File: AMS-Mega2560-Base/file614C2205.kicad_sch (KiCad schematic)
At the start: 3 parts, among them IC1 CD74HC4050ME4, IC2 CD74HC4050ME4, J8 Conn_01x03

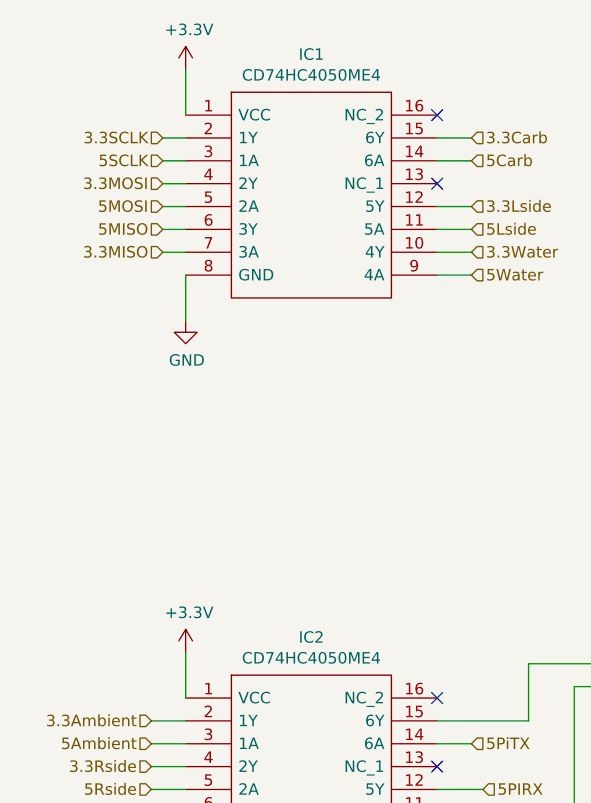
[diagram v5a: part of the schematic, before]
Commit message: WIP for power on input and RTC battery switch over.
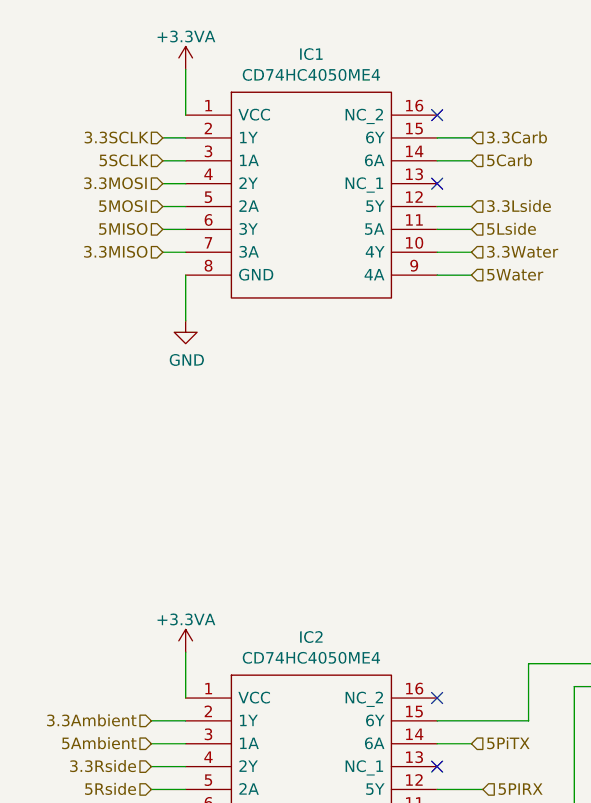
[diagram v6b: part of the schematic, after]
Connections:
- net +3V3 renamed +3.3VA
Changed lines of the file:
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@@
     (pin "9")
-  )
-  (symbol (lib_id "power:+3.3V") (at 53.34 33.02 0) (unit 1)
-    (in_bom yes) (on_board yes)
-    (property "Reference" "#PWR017" (id 0) (at 53.34 36.83 0)
-      (effects (font (size 1.27 1.27)) hide)
-    )
-    (property "Value" "+3.3V" (id 1) (at 53.721 28.6258 0))
-    (property "Footprint" "" (id 2) (at 53.34 33.02 0)
-      (effects (font (size 1.27 1.27)) hide)
-    )
-    (property "Datasheet" "" (id 3) (at 53.34 33.02 0)
-      (effects (font (size 1.27 1.27)) hide)
-    )
-    (pin "1")
   )
   (symbol (lib_id "power:GND") (at 53.34 60.96 0) (unit 1)
@@
     (pin "9")
   )
-  (symbol (lib_id "power:+3.3V") (at 53.34 97.79 0) (unit 1)
-    (in_bom yes) (on_board yes)
-    (property "Reference" "#PWR019" (id 0) (at 53.34 101.6 0)
-      (effects (font (size 1.27 1.27)) hide)
-    )
-    (property "Value" "+3.3V" (id 1) (at 53.721 93.3958 0))
-    (property "Footprint" "" (id 2) (at 53.34 97.79 0)
-      (effects (font (size 1.27 1.27)) hide)
-    )
-    (property "Datasheet" "" (id 3) (at 53.34 97.79 0)
-      (effects (font (size 1.27 1.27)) hide)
-    )
-    (pin "1")
-  )
   (symbol (lib_id "power:GND") (at 53.34 125.73 0) (unit 1)
     (in_bom yes) (on_board yes)
@@
       (effects (font (size 1.27 1.27)) hide)
     )
+    (pin "1")
+  )
+  (symbol (lib_id "power:+3.3VA") (at 53.34 33.02 0) (mirror y) (unit 1)
+    (in_bom yes) (on_board yes) (fields_autoplaced)
+    (property "Reference" "#PWR0132" (id 0) (at 53.34 36.83 0)
+      (effects (font (size 1.27 1.27)) hide)
+    )
+    (property "Value" "+3.3VA" (id 1) (at 53.34 29.4155 0))
+    (property "Footprint" "" (id 2) (at 53.34 33.02 0)
+      (effects (font (size 1.27 1.27)) hide)
+    )
+    (property "Datasheet" "" (id 3) (at 53.34 33.02 0)
+      (effects (font (size 1.27 1.27)) hide)
+    )
+    (pin "1")
+  )
+  (symbol (lib_id "power:+3.3VA") (at 53.34 97.79 0) (mirror y) (unit 1)
+    (in_bom yes) (on_board yes) (fields_autoplaced)
+    (property "Reference" "#PWR0133" (id 0) (at 53.34 101.6 0)
+      (effects (font (size 1.27 1.27)) hide)
+    )
+    (property "Value" "+3.3VA" (id 1) (at 53.34 94.1855 0))
+    (property "Footprint" "" (id 2) (at 53.34 97.79 0)
+      (effects (font (size 1.27 1.27)) hide)
+    )
+    (property "Datasheet" "" (id 3) (at 53.34 97.79 0)
+      (effects (font (size 1.27 1.27)) hide)
+    )
